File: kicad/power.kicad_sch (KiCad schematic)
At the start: 44 parts, among them J5 Conn_Coaxial_Power, J6 Screw_Terminal_01x02, U11 ADP7118ACPZN, U22 ADP7118ACPZN, U24 MIC2025-2YM, U7 LTM8078EY-PBF, U8 ADP7118ACPZN, U9 ADP7118ACPZN

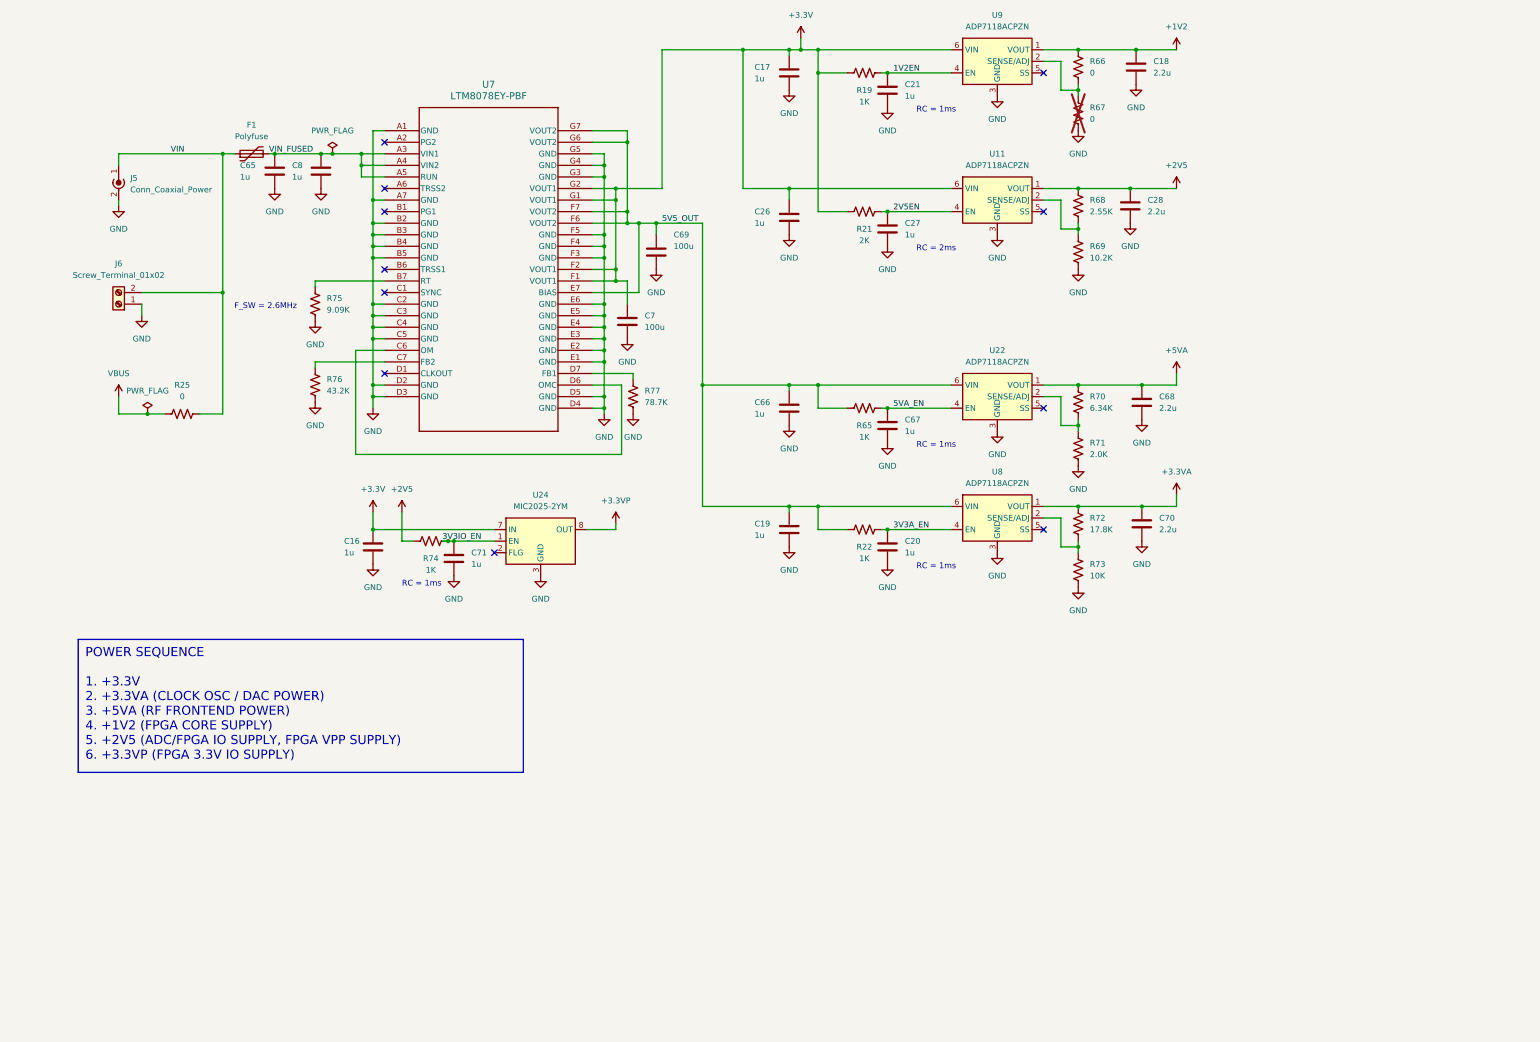
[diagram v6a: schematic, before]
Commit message: swap ice40 for max v, add 1.2v switcher
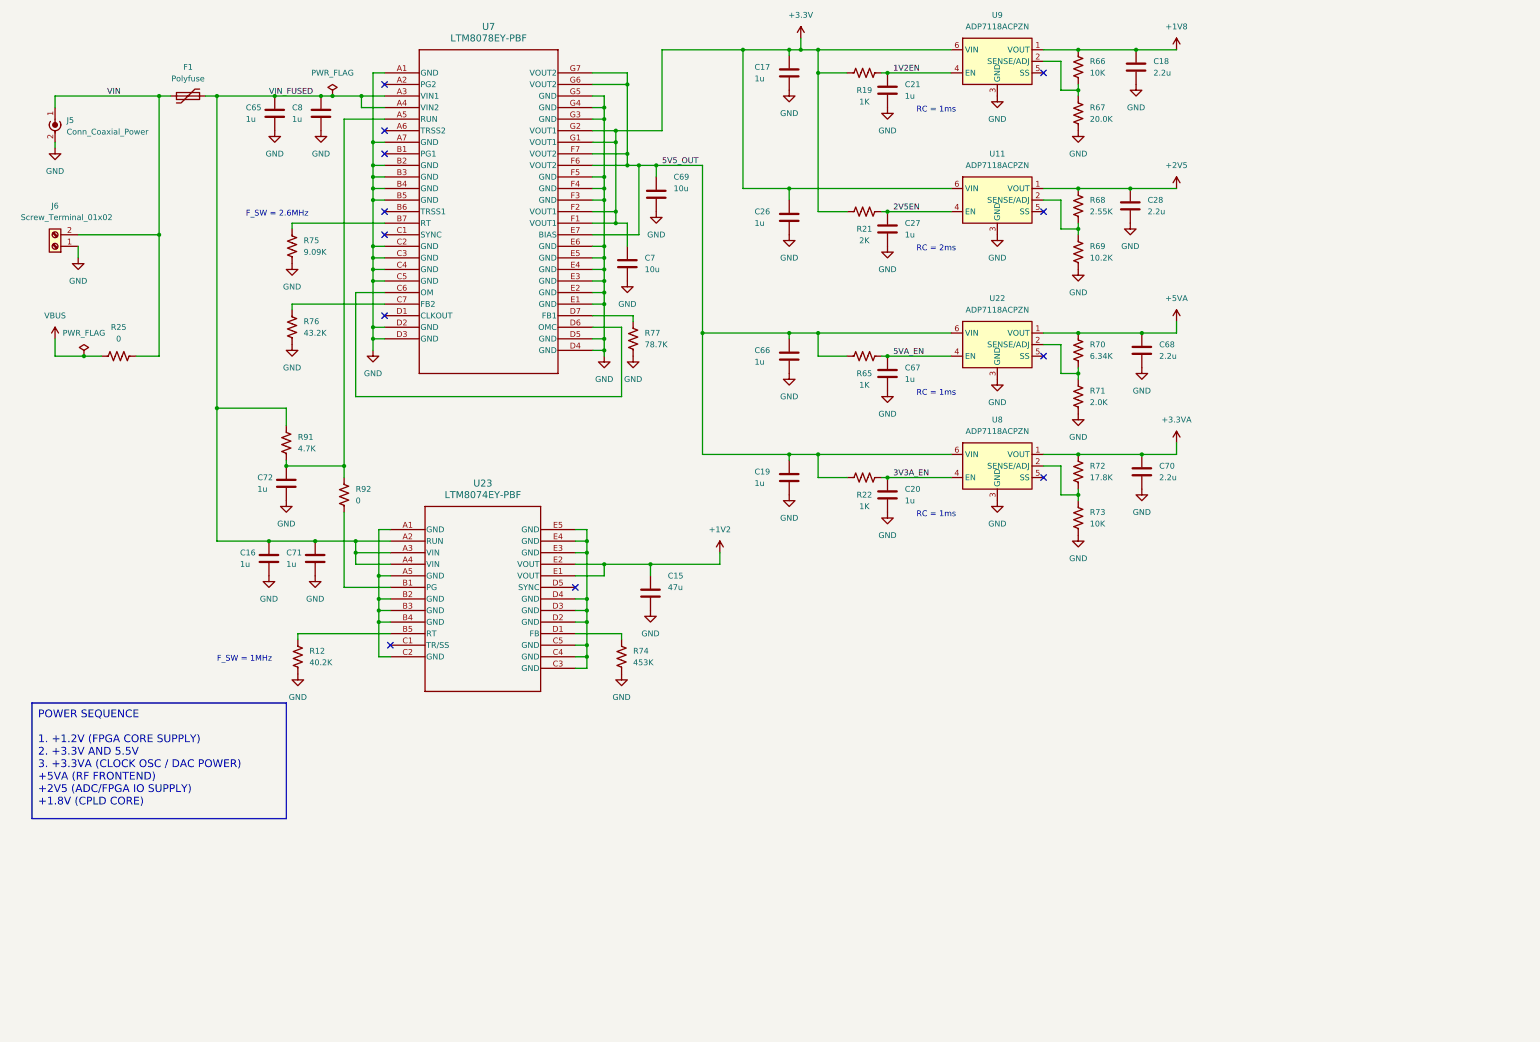
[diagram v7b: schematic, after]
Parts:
- removed U24: MIC2025-2YM, Package_SO:SOIC-8_3.9x4.9mm_P1.27mm, symbol Power_Management:MIC2025-2YM
- added C15: 47u, symbol Device:C
- added C72: 1u, symbol Device:C
- added R12: 40.2K, symbol Device:R_US
- added R91: 4.7K, symbol Device:R_US
- added R92: 0, symbol Device:R_US
- added U23: LTM8074EY-PBF, 05-08-1566_ADI, symbol bgelb_lib:LTM8074EY-PBF
- C69, C7: value 100u -> 10u
- R66: value 0 -> 10K
- R67: value 0 -> 20.0K; now fitted
- R74: value 1K -> 453K
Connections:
- net +1V2: now also C15.1, U23.E1 (VOUT), U23.E2 (VOUT); no longer C18.1, R66.1, U9.1 (VOUT)
- net +2V5: no longer R74.1
- net +3.3V: no longer C16.1
- net GND: now also R74.2, C15.2, C72.2, R12.2
- net VIN_FUSED: now also C16.1, C71.1, R91.1, U23.A2 (RUN), U23.A3 (VIN), U23.A4 (VIN); no longer U7.A5 (RUN)
- removed net 3V3IO_EN: C71.1, R74.2
- new net: C72.1, R91.2, R92.1, U7.A5 (RUN)
- new net: R92.2, U23.B1 (PG)
- new net: R12.1, U23.B5 (RT)
- new net: U23.A1 (GND), U23.A5 (GND), U23.B2 (GND), U23.B3 (GND), U23.B4 (GND), U23.C2 (GND)
- new net: U23.C3 (GND), U23.C4 (GND), U23.C5 (GND), U23.D2 (GND), U23.D3 (GND), U23.D4 (GND), U23.E3 (GND), U23.E4 (GND), U23.E5 (GND)
- new net: R74.1, U23.D1 (FB)
- new net +1V8: C18.1, R66.1, U9.1 (VOUT)
- no-connect marks 11 -> 12
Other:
- note added: "F_SW = 1MHz"
- moved on the sheet: C19, C20, C65, C66, C67, C68, C69, C7, C70, C8, F1, J5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

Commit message: add lte radio and various fixes
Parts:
- removed R25: 0, symbol Device:R_US
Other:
- moved on the sheet: C15, C16, C17, C18, C19, C20, C21, C26, C27, C28, C65, C66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
